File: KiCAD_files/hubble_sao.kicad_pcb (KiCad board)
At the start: 2 copper layers, 38 x 45.5 mm, 41 parts, among them J1 Conn_02x03_Counter_Clockwise, J2 Conn_02x03_Odd_Even, Q1 DMP3099L-7, SW1 SW_Push_Shielded, U1 VEML3328, U2 LSM6DSO, U3 ATmega328PB-A, U4 AD8532, U5 AD8532

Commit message: Corrected the input wiring of the opamps (schematic & pcb)
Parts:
- C6: value C -> 100nF
- L1: value L -> 10uH
- R1: value R -> 220
- R9: value R -> 15
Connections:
- C10 pad 1: Net-(D1-K) -> Net-(D3-K)
- C14 pad 1: Net-(D2-K) (its old number) -> Net-(D1-K)
- C8 pad 1: Net-(D3-K) -> Net-(D4-K)
- C9 pad 1: Net-(D4-K) -> Net-(D5-K)
- D1 pad 1: Net-(D2-K) (its old number) -> Net-(D1-K)
- D3 pad 1: Net-(D1-K) -> Net-(D3-K)
- D4 pad 1: Net-(D3-K) -> Net-(D4-K)
- D5 pad 1: Net-(D4-K) -> Net-(D5-K)
- R10 pad 1: Net-(D1-K) -> Net-(D3-K)
- R3 pad 1: Net-(D3-K) -> Net-(D4-K)
- R4 pad 1: Net-(D4-K) -> Net-(D5-K)
- R5 pad 1: Net-(D2-K) (its old number) -> Net-(D1-K)
- U4 pad 2: GND -> Net-(D4-K)
- U4 pad 3: Net-(D3-K) -> GND
- U4 pad 5: Net-(D4-K) -> GND
- U4 pad 6: GND -> Net-(D5-K)
- U5 pad 2: GND -> Net-(D3-K)
- U5 pad 3: Net-(D1-K) -> GND
- U5 pad 5: Net-(D2-K) (its old number) -> GND
- U5 pad 6: GND -> Net-(D1-K)
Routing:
- net Net-(D5-K): track 0.00 -> 10.8 mm, vias 0 -> 1
- net Net-(D2-K) (its old number): track 10.4 -> 0.00 mm, vias 1 -> 0
- net Net-(D4-K): track 10.6 -> 12.0 mm
- net Net-(D3-K): track 11.4 -> 12.1 mm
- net GND: vias 30 -> 26

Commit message: Changed opamp from AD8532 to TLV9062D
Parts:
- U4, U5: value AD8532 -> TLV9062xD
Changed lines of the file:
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@@
 			)
 		)
-		(property "Value" "AD8532"
+		(property "Value" "TLV9062xD"
 			(at 0 -3.4 90)
 			(layer "B.Fab")
@@
 			)
 		)
-		(property "Datasheet" "https://www.analog.com/media/en/technical-documentation/data-sheets/AD8531_8532_8534.pdf"
+		(property "Datasheet" "https://www.ti.com/lit/ds/symlink/tlv9062.pdf"
 			(at 0 0 90)
 			(unlocked yes)
@@
 			)
 		)
-		(property "Description" "Dual Operational Amplifiers"
+		(property "Description" "Dual operational amplifier, 300 uV Offset, SOIC-8"
 			(at 0 0 90)
 			(unlocked yes)
@@
 			)
 		)
+		(property ki_fp_filters "SOIC*3.9x4.9mm*P1.27mm*")
 		(sheetname "Root")
 		(sheetfile "hubble_sao.kicad_sch")
@@
 			)
 		)
-		(property "Value" "AD8532"
+		(property "Value" "TLV9062xD"
 			(at 0 -3.4 90)
 			(layer "B.Fab")
@@
 			)
 		)
-		(property "Datasheet" "https://www.analog.com/media/en/technical-documentation/data-sheets/AD8531_8532_8534.pdf"
+		(property "Datasheet" "https://www.ti.com/lit/ds/symlink/tlv9062.pdf"
 			(at 0 0 -90)
 			(unlocked yes)
@@
 			)
 		)
-		(property "Description" "Dual Operational Amplifiers"
+		(property "Description" "Dual operational amplifier, 300 uV Offset, SOIC-8"
 			(at 0 0 -90)
 			(unlocked yes)
@@
 			)
 		)
+		(property ki_fp_filters "SOIC*3.9x4.9mm*P1.27mm*")
 		(sheetname "Root")
 		(sheetfile "hubble_sao.kicad_sch")

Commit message: FIX: Corrected the pMOSFET wiring. Fixes #1
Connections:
- Q1 pad 2: Net-(D2-A) -> VCC
- Q1 pad 3: VCC -> Net-(D2-A)
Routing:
- net VCC: track 158.3 -> 156.9 mm
- net Net-(D2-A): track 5.13 -> 4.06 mm
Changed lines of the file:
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@@
 			(layers "B.Cu" "B.Paste" "B.Mask")
 			(roundrect_rratio 0.25)
-			(net 9 "Net-(D2-A)")
+			(net 18 "VCC")
 			(pinfunction "S")
 			(pintype "passive")
@@
 			(layers "B.Cu" "B.Paste" "B.Mask")
 			(roundrect_rratio 0.25)
-			(net 18 "VCC")
+			(net 9 "Net-(D2-A)")
 			(pinfunction "D")
 			(pintype "passive")
@@
 		)
 		(layer "F.Cu")
+		(net 3)
 	)
 	(gr_arc
@@
 		)
 		(layer "F.Cu")
+		(net 3)
 	)
 	(gr_arc
@@
 		)
 		(layer "F.Cu")
+		(net 3)
 	)
 	(gr_arc
@@
 		)
 		(layer "F.Cu")
+		(net 9)
 	)
 	(gr_poly
@@
 	)
 	(segment
-		(start 79.75969 123.423131)
-		(end 79.430871 123.75195)
+		(start 79.776463 123.715336)
+		(end 79.739849 123.75195)
 		(width 0.2)
 		(layer "F.Cu")
@@
 	)
 	(segment
-		(start 79.430871 123.75195)
+		(start 79.739849 123.75195)
 		(end 79.40831 123.75195)
 		(width 0.2)
@@
 	)
 	(segment
-		(start 79.75969 122.95969)
-		(end 79.75969 123.423131)
-		(width 0.2)
-		(layer "F.Cu")
-		(net 9)
-	)
-	(segment
 		(start 76.5 122.6)
 		(end 76.5 121.5)
@@
 	)
 	(via
-		(at 79.75969 122.95969)
+		(at 79.776463 123.715336)
 		(size 0.7)
 		(drill 0.3)
@@
 	)
 	(segment
-		(start 79.96938 122.75)
-		(end 82.75 122.75)
+		(start 80.530761 121.8)
+		(end 80.875 121.8)
+		(width 0.2)
+		(layer "B.Cu")
+		(net 9)
+	)
+	(segment
+		(start 79.776463 123.715336)
+		(end 79.776463 122.554298)
 		(width 0.2)
 		(layer "B.Cu")
@@
 	)
 	(segment
-		(start 79.75969 122.95969)
-		(end 79.96938 122.75)
+		(start 79.776463 122.554298)
+		(end 80.530761 121.8)
 		(width 0.2)
 		(layer "B.Cu")
@@
 	)
 	(segment
+		(start 80.5 122.75)
+		(end 80.5 120)
+		(width 0.3)
+		(layer "F.Cu")
+		(net 18)
+	)
+	(segment
 		(start 92.25 131.25)
 		(end 91.1 131.25)
@@
 	)
 	(segment
-		(start 80.5 136.25)
-		(end 80.5 120)
-		(width 0.3)
-		(layer "F.Cu")
-		(net 18)
-	)
-	(segment
 		(start 81 137.75)
 		(end 81.5 137.25)
@@
 	)
 	(segment
+		(start 80.5 136.25)
+		(end 80.5 122.75)
+		(width 0.3)
+		(layer "F.Cu")
+		(net 18)
+	)
+	(segment
 		(start 80.5 120)
 		(end 80.5 118.5)
@@
 	)
 	(via
-		(at 80.5 120)
+		(at 92 107.25)
 		(size 0.7)
 		(drill 0.3)
@@
 	)
 	(via
-		(at 92 107.25)
+		(at 87.7 130)
 		(size 0.7)
 		(drill 0.3)
 		(layers "F.Cu" "B.Cu")
-		(free yes)
 		(net 18)
 	)
 	(via
-		(at 87.7 130)
+		(at 92.25 131.25)
 		(size 0.7)
 		(drill 0.3)
@@
 	)
 	(via
-		(at 92.25 131.25)
+		(at 80.5 122.75)
 		(size 0.7)
 		(drill 0.3)
@@
 	)
 	(segment
-		(start 80.5 120.75)
-		(end 80.875 121.125)
-		(width 0.2)
-		(layer "B.Cu")
-		(net 18)
-	)
-	(segment
 		(start 104.58 107.25)
 		(end 106.08 108.75)
@@
 	)
 	(segment
-		(start 80.875 121.125)
-		(end 80.875 121.8)
-		(width 0.2)
-		(layer "B.Cu")
-		(net 18)
-	)
-	(segment
 		(start 88.5 103.2125)
 		(end 88.5 104.75)
@@
 	)
 	(segment
+		(start 82.75 122.75)
+		(end 80.5 122.75)
+		(width 0.3)
+		(layer "B.Cu")
+		(net 18)
+	)
+	(segment
 		(start 92.25 131.25)
 		(end 92.25 130.75)
@@
 	)
 	(segment
-		(start 80.4625 120.0375)
-		(end 78.75 120.0375)
-		(width 0.2)
-		(layer "B.Cu")
-		(net 18)
-	)
-	(segment
 		(start 92 129.5)
 		(end 92 130.5)
@@
 	)
 	(segment
-		(start 80.5 120)
-		(end 80.5 120.75)
-		(width 0.2)
-		(layer "B.Cu")
-		(net 18)
-	)
-	(segment
 		(start 82.5 143)
 		(end 83.4 143.9)
 		(width 0.3)
 		(layer "B.Cu")
-		(net 18)
-	)
-	(segment
-		(start 80.5 120)
-		(end 80.4625 120.0375)
-		(width 0.3)
-		(layer "B.Cu")

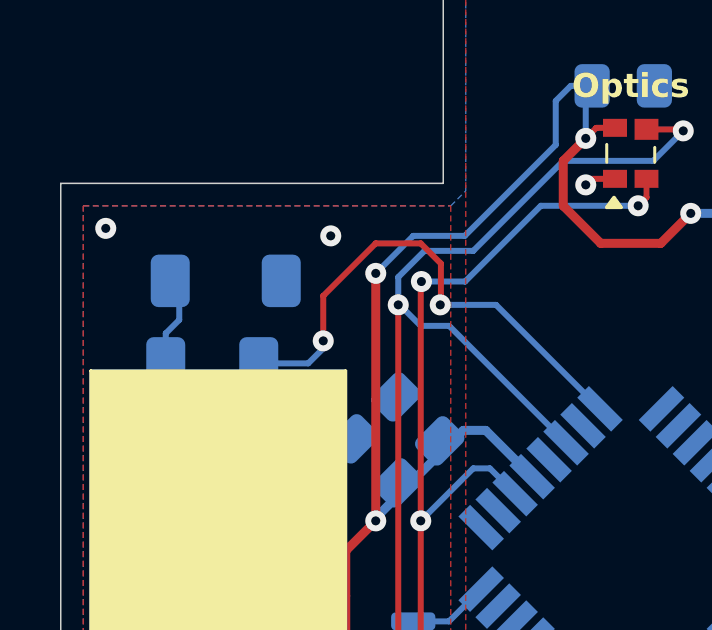
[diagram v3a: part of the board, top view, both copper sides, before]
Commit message: Simplified the blinky LED's traces
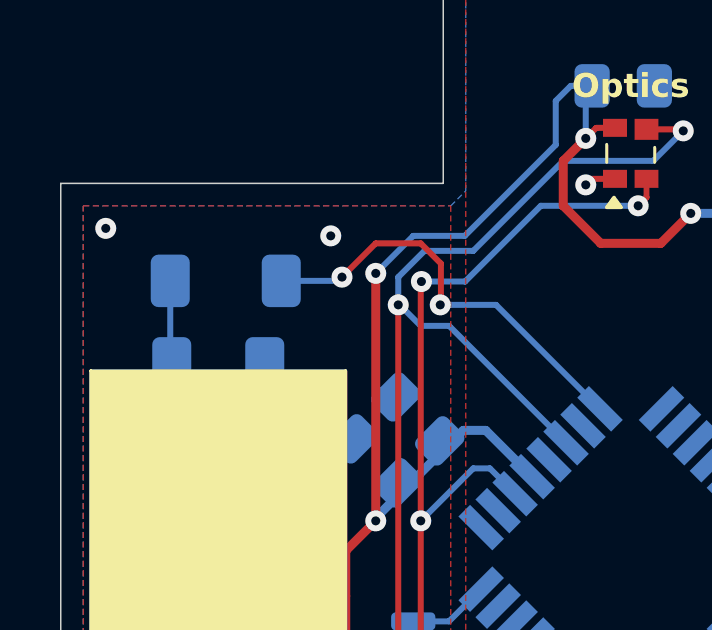
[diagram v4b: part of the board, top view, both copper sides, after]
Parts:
- moved R1 0.20 mm to (76.2, 112.2), turned to 180 degrees
- turned D6 to 0 degrees
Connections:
- D6 pad 1: GND -> Net-(D6-K)
- D6 pad 2: Net-(D6-A) -> /LED
- R1 pad 1: Net-(D6-A) -> GND
- R1 pad 2: /LED -> Net-(D6-K)
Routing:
- net Net-(D6-A): track 2.94 -> 0.00 mm
- net Net-(D6-K): track 0.00 -> 2.77 mm
- net /LED: track 16.7 -> 14.3 mm
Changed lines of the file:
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@@
 	(net 4 "Net-(U3-AVCC)")
 	(net 5 "/SCK")
-	(net 6 "Net-(D6-A)")
+	(net 6 "Net-(D6-K)")
 	(net 7 "Net-(U3-AREF)")
 	(net 8 "/BUTTON")
@@
 	(footprint "Resistor_SMD:R_1206_3216Metric_Pad1.30x1.75mm_HandSolder"
 		(layer "B.Cu")
-		(at 76.05 112.25)
+		(at 76.25 112.25 180)
 		(descr "Resistor SMD 1206 (3216 Metric), square (rectangular) end terminal, IPC_7351 nominal with elongated pad for handsoldering. (Body size source: IPC-SM-782 page 72, https://www.pcb-3d.com/wordpress/wp-content/uploads/ipc-sm-782a_amendment_1_and_2.pdf), generated with kicad-footprint-generator")
 		(tags "resistor handsolder")
 		(property "Reference" "R1"
-			(at -3.3 0 0)
+			(at -3.3 0 360)
 			(layer "B.SilkS")
 			(effects
@@
 		)
 		(property "Value" "220"
-			(at 0 -1.82 0)
+			(at 0 -1.82 360)
 			(layer "B.Fab")
 			(effects
@@
 		)
 		(property "Footprint" "Resistor_SMD:R_1206_3216Metric_Pad1.30x1.75mm_HandSolder"
-			(at 0 0 180)
+			(at 0 0 0)
 			(unlocked yes)
 			(layer "B.Fab")
@@
 		)
 		(property "Datasheet" ""
-			(at 0 0 180)
+			(at 0 0 0)
 			(unlocked yes)
 			(layer "B.Fab")
@@
 		)
 		(property "Description" "Resistor"
-			(at 0 0 180)
+			(at 0 0 0)
 			(unlocked yes)
 			(layer "B.Fab")
@@
 		(attr smd)
 		(fp_line
-			(start 0.727064 -0.91)
-			(end -0.727064 -0.91)
+			(start 0.727064 0.91)
+			(end -0.727064 0.91)
 			(stroke
 				(width 0.12)
@@
 		)
 		(fp_line
-			(start 0.727064 0.91)
-			(end -0.727064 0.91)
+			(start 0.727064 -0.91)
+			(end -0.727064 -0.91)
 			(stroke
 				(width 0.12)
@@
 		)
 		(fp_line
-			(start -2.45 -1.12)
-			(end 2.45 -1.12)
+			(start 2.45 1.12)
+			(end -2.45 1.12)
 			(stroke
 				(width 0.05)
@@
 		)
 		(fp_line
-			(start -2.45 1.12)
-			(end -2.45 -1.12)
+			(start 2.45 -1.12)
+			(end 2.45 1.12)
 			(stroke
 				(width 0.05)
@@
 		)
 		(fp_line
-			(start 2.45 -1.12)
-			(end 2.45 1.12)
+			(start -2.45 1.12)
+			(end -2.45 -1.12)
 			(stroke
 				(width 0.05)
@@
 		)
 		(fp_line
-			(start 2.45 1.12)
-			(end -2.45 1.12)
+			(start -2.45 -1.12)
+			(end 2.45 -1.12)
 			(stroke
 				(width 0.05)
@@
 		)
 		(fp_line
-			(start -1.6 -0.8)
-			(end 1.6 -0.8)
+			(start 1.6 0.8)
+			(end -1.6 0.8)
 			(stroke
 				(width 0.1)
@@
 		)
 		(fp_line
-			(start -1.6 0.8)
-			(end -1.6 -0.8)
+			(start 1.6 -0.8)
+			(end 1.6 0.8)
 			(stroke
 				(width 0.1)
@@
 		)
 		(fp_line
-			(start 1.6 -0.8)
-			(end 1.6 0.8)
+			(start -1.6 0.8)
+			(end -1.6 -0.8)
 			(stroke
 				(width 0.1)
@@
 		)
 		(fp_line
-			(start 1.6 0.8)
-			(end -1.6 0.8)
+			(start -1.6 -0.8)
+			(end 1.6 -0.8)
 			(stroke
 				(width 0.1)
@@
 		)
 		(fp_text user "${REFERENCE}"
-			(at -3.3 0 0)
+			(at -3.3 0 360)
 			(layer "B.Fab")
 			(effects
@@
 		)
 		(pad "1" smd roundrect
-			(at -1.55 0)
+			(at -1.55 0 180)
 			(size 1.3 1.75)
 			(layers "B.Cu" "B.Paste" "B.Mask")
 			(roundrect_rratio 0.192308)
-			(net 6 "Net-(D6-A)")
+			(net 20 "GND")
 			(pintype "passive")
 		)
 		(pad "2" smd roundrect
-			(at 1.55 0)
+			(at 1.55 0 180)
 			(size 1.3 1.75)
 			(layers "B.Cu" "B.Paste" "B.Mask")
 			(roundrect_rratio 0.192308)
-			(net 14 "/LED")
+			(net 6 "Net-(D6-K)")
 			(pintype "passive")
 		)
@@
 	(footprint "LED_SMD:LED_1206_3216Metric_ReverseMount_Hole1.8x2.4mm"
 		(layer "B.Cu")
-		(at 76.5 109.5 180)
+		(at 76.5 109.5)
 		(descr "LED SMD 1206 (3216 Metric), reverse mount, square (rectangular) end terminal, IPC_7351 nominal, (Body size source: http://www.tortai-tech.com/upload/download/2011102023233369053.pdf), generated with kicad-footprint-generator")
 		(tags "diode reverse")
 		(property "Reference" "D6"
-			(at 3.75 -0.25 0)
+			(at 3.75 -0.25 360)
 			(layer "B.SilkS")
 			(effects
@@
 		)
 		(property "Value" "LED"
-			(at 0 -2.145 0)
+			(at 0 -2.145 360)
 			(layer "B.Fab")
 			(effects
@@
 		)
 		(property "Footprint" "LED_SMD:LED_1206_3216Metric_ReverseMount_Hole1.8x2.4mm"
-			(at 0 0 0)
+			(at 0 0 180)
 			(unlocked yes)
 			(layer "B.Fab")
@@
 		)
 		(property "Datasheet" ""
-			(at 0 0 0)
+			(at 0 0 180)
 			(unlocked yes)
 			(layer "B.Fab")
@@
 		)
 		(property "Description" "Light emitting diode"
-			(at 0 0 0)
+			(at 0 0 180)
 			(unlocked yes)
 			(layer "B.Fab")
@@
 		(attr smd)
 		(fp_line
-			(start 1.6 -1.46)
-			(end -2.8 -1.46)
+			(start -2.8 -1.45)
+			(end -2.8 1.45)
 			(stroke
 				(width 0.12)
@@
 		)
 		(fp_line
-			(start -2.8 -1.45)
-			(end -2.8 1.45)
+			(start 1.6 -1.46)
+			(end -2.8 -1.46)
 			(stroke
 				(width 0.12)
@@
 		)
 		(fp_line
-			(start 2.65 1.46)
-			(end -2.8 1.46)
+			(start -2.8 -1.46)
+			(end 2.65 -1.46)
 			(stroke
 				(width 0.05)
@@
 		)
 		(fp_line
-			(start 2.65 -1.46)
-			(end 2.65 1.46)
+			(start -2.8 1.47)
+			(end -2.8 -1.45)
 			(stroke
 				(width 0.05)
@@
 		)
 		(fp_line
-			(start -2.8 1.47)
-			(end -2.8 -1.45)
+			(start 2.65 -1.46)
+			(end 2.65 1.46)
 			(stroke
 				(width 0.05)
@@
 		)
 		(fp_line
-			(start -2.8 -1.46)
-			(end 2.65 -1.46)
+			(start 2.65 1.46)
+			(end -2.8 1.46)
 			(stroke
 				(width 0.05)
@@
 		)
 		(fp_line
-			(start 1.6 0.8)
-			(end 1.6 -0.8)
+			(start -1.6 -0.8)
+			(end -1.6 0.4)
 			(stroke
 				(width 0.1)
@@
 		)
 		(fp_line
-			(start 1.6 -0.8)
-			(end -1.6 -0.8)
+			(start -1.6 0.4)
+			(end -1.2 0.8)
 			(stroke
 				(width 0.1)
@@
 		)
 		(fp_line
-			(start -1.6 0.4)
-			(end -1.2 0.8)
+			(start 1.6 -0.8)
+			(end -1.6 -0.8)
 			(stroke
 				(width 0.1)
@@
 		)
 		(fp_line
-			(start -1.6 -0.8)
-			(end -1.6 0.4)
+			(start 1.6 0.8)
+			(end 1.6 -0.8)
 			(stroke
 				(width 0.1)
@@
 		)
 		(fp_text user "${REFERENCE}"
-			(at 0 0 0)
+			(at 0 0 360)
 			(layer "B.Fab")
 			(effects
@@
 		)
 		(pad "" np_thru_hole oval
-			(at 0 0 180)
+			(at 0 0)
 			(size 1.8 2.4)
 			(drill oval 1.8 2.4)
@@
 		)
 		(pad "1" smd roundrect
-			(at -1.85 0 180)
+			(at -1.85 0)
 			(size 1.3 1.75)
 			(layers "B.Cu" "B.Paste" "B.Mask")
 			(roundrect_rratio 0.2)
-			(net 20 "GND")
+			(net 6 "Net-(D6-K)")
 			(pinfunction "K")
 			(pintype "passive")
 		)
 		(pad "2" smd roundrect
-			(at 1.85 0 180)
+			(at 1.85 0)
 			(size 1.3 1.75)
 			(layers "B.Cu" "B.Paste" "B.Mask")
 			(roundrect_rratio 0.2)
-			(net 6 "Net-(D6-A)")
+			(net 14 "/LED")
 			(pinfunction "A")
 			(pintype "passive")
@@
 	)
 	(segment
-		(start 74.95 110.8)
-		(end 74.95 109.5)
+		(start 74.65 112.2)
+		(end 74.7 112.25)
 		(width 0.2)
 		(layer "B.Cu")
@@
 	)
 	(segment
-		(start 74.5 111.25)
-		(end 74.95 110.8)
-		(width 0.2)
-		(layer "B.Cu")
-		(net 6)
-	)
-	(segment
-		(start 74.5 112.25)
-		(end 74.5 111.25)
+		(start 74.65 109.5)
+		(end 74.65 112.2)
 		(width 0.2)
 		(layer "B.Cu")
@@
 	)
 	(segment
-		(start 81.5 108.25)
-		(end 83 108.25)
-		(width 0.2)
-		(layer "F.Cu")
-		(net 14)
-	)
-	(segment
-		(start 79.75 111.5)
-		(end 79.75 110)
+		(start 83 108.25)
+		(end 83.67212 108.92212)
 		(width 0.2)
 		(layer "F.Cu")
@@
 	)
 	(segment
-		(start 79.75 110)
+		(start 80.375 109.375)
 		(end 81.5 108.25)
 		(width 0.2)
@@
 	)
 	(segment
-		(start 83 108.25)
-		(end 83.67212 108.92212)
+		(start 83.67212 108.92212)
+		(end 83.67212 110.27788)
 		(width 0.2)
 		(layer "F.Cu")
@@
 	)
 	(segment
-		(start 83.67212 108.92212)
-		(end 83.67212 110.27788)
+		(start 81.5 108.25)
+		(end 83 108.25)
 		(width 0.2)
 		(layer "F.Cu")
@@
 	)
 	(via
-		(at 79.75 111.5)
+		(at 80.375 109.375)
 		(size 0.7)
 		(drill 0.3)
@@
 	)
 	(segment
-		(start 79.75 111.5)
-		(end 79.75 111.75)
-		(width 0.2)
-		(layer "B.Cu")
-		(net 14)
-	)
-	(segment
-		(start 79.75 111.75)
-		(end 79.25 112.25)
+		(start 83.65 110.3)
+		(end 85.509798 110.3)
 		(width 0.2)
 		(layer "B.Cu")
@@
 	)
 	(segment
-		(start 79.25 112.25)
-		(end 78.1 112.25)
+		(start 80.25 109.5)
+		(end 80.375 109.375)
 		(width 0.2)
 		(layer "B.Cu")
@@
 	)
 	(segment
-		(start 83.65 110.3)
-		(end 85.509798 110.3)
+		(start 85.509798 110.3)
+		(end 88.974695 113.764897)
 		(width 0.2)
 		(layer "B.Cu")
@@
 	)
 	(segment
-		(start 85.509798 110.3)
-		(end 88.974695 113.764897)
+		(start 78.35 109.5)
+		(end 80.25 109.5)
 		(width 0.2)
 		(layer "B.Cu")

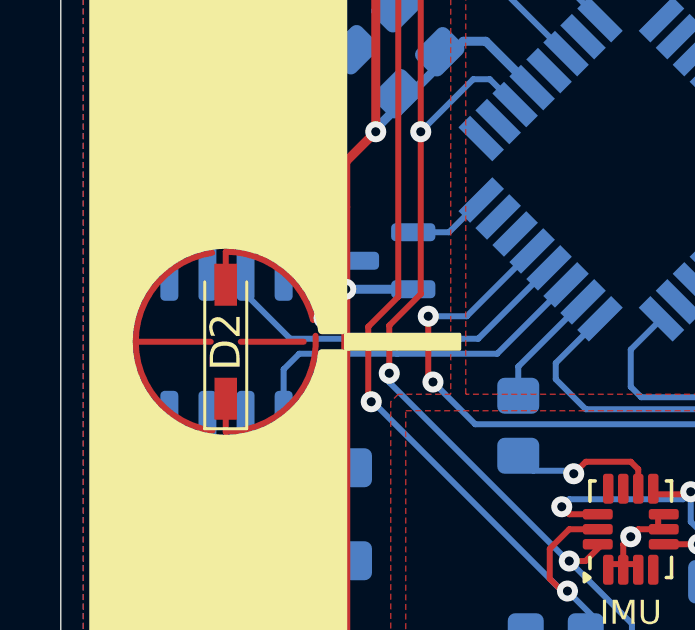
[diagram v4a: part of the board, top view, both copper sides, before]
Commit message: Fixed DRC errors
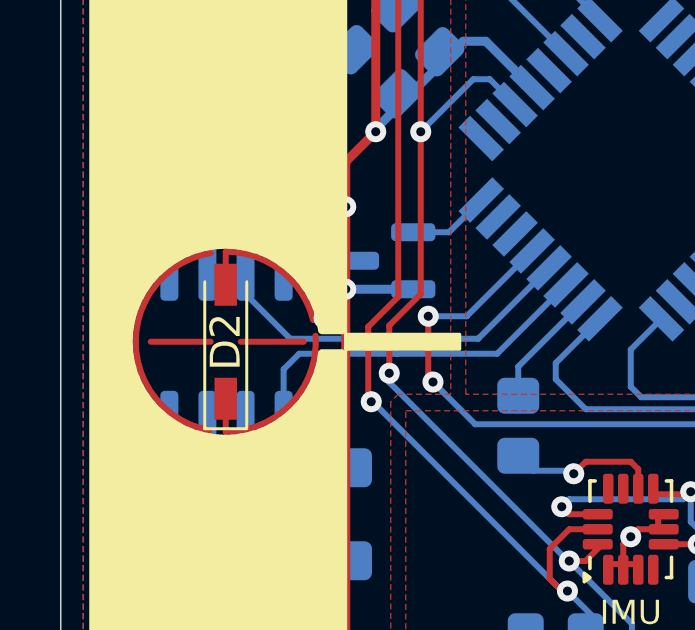
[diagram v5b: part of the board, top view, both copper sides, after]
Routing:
- net VCC: track 156.9 -> 158.6 mm, vias 14 -> 15
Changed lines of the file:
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@@
 	)
 	(gr_arc
-		(start 73.5 124.5)
-		(mid 74.224348 122.545158)
-		(end 76.047606 121.534306)
+		(start 75.963344 127.45161)
+		(mid 74.196745 126.422243)
+		(end 73.5 124.5)
 		(stroke
 			(width 0.2)
@@
 		)
 		(layer "F.Cu")
-		(net 3)
-	)
-	(gr_arc
-		(start 76.054979 127.466809)
-		(mid 74.22678 126.457669)
-		(end 73.5 124.5)
-		(stroke
-			(width 0.2)
-			(type default)
-		)
-		(layer "F.Cu")
-		(net 3)
 	)
 	(gr_arc
@@
 	)
 	(gr_line
-		(start 73.5 124.5)
+		(start 74 124.5)
 		(end 76 124.5)
 		(stroke
@@
 		)
 		(layer "F.Cu")
-		(net 3)
 	)
 	(gr_arc
@@
 		(net 3)
 	)
+	(gr_arc
+		(start 73.5 124.5)
+		(mid 74.21094 122.560875)
+		(end 76.006803 121.540818)
+		(stroke
+			(width 0.2)
+			(type default)
+		)
+		(layer "F.Cu")
+	)
 	(gr_line
 		(start 77 124.5)
@@
 		)
 		(layer "F.Cu")
-		(net 9)
 	)
 	(gr_poly
@@
 	)
 	(via
+		(at 80.5 120)
+		(size 0.7)
+		(drill 0.3)
+		(layers "F.Cu" "B.Cu")
+		(net 18)
+	)
+	(via
 		(at 81 141.6)
 		(size 0.7)
@@
 	)
 	(segment
+		(start 80.4625 120.0375)
+		(end 80.5 120)
+		(width 0.3)
+		(layer "B.Cu")
+		(net 18)
+	)
+	(segment
 		(start 82.5 143)
 		(end 83.4 143.9)
@@
 		(layer "B.Cu")
 		(net 18)
+	)
+	(segment
+		(start 78.75 120.0375)
+		(end 80.4625 120.0375)
+		(width 0.3)
+		(layer "B.Cu")
+		(net 18)
